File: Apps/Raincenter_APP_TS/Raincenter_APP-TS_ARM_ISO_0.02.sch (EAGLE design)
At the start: 26 parts

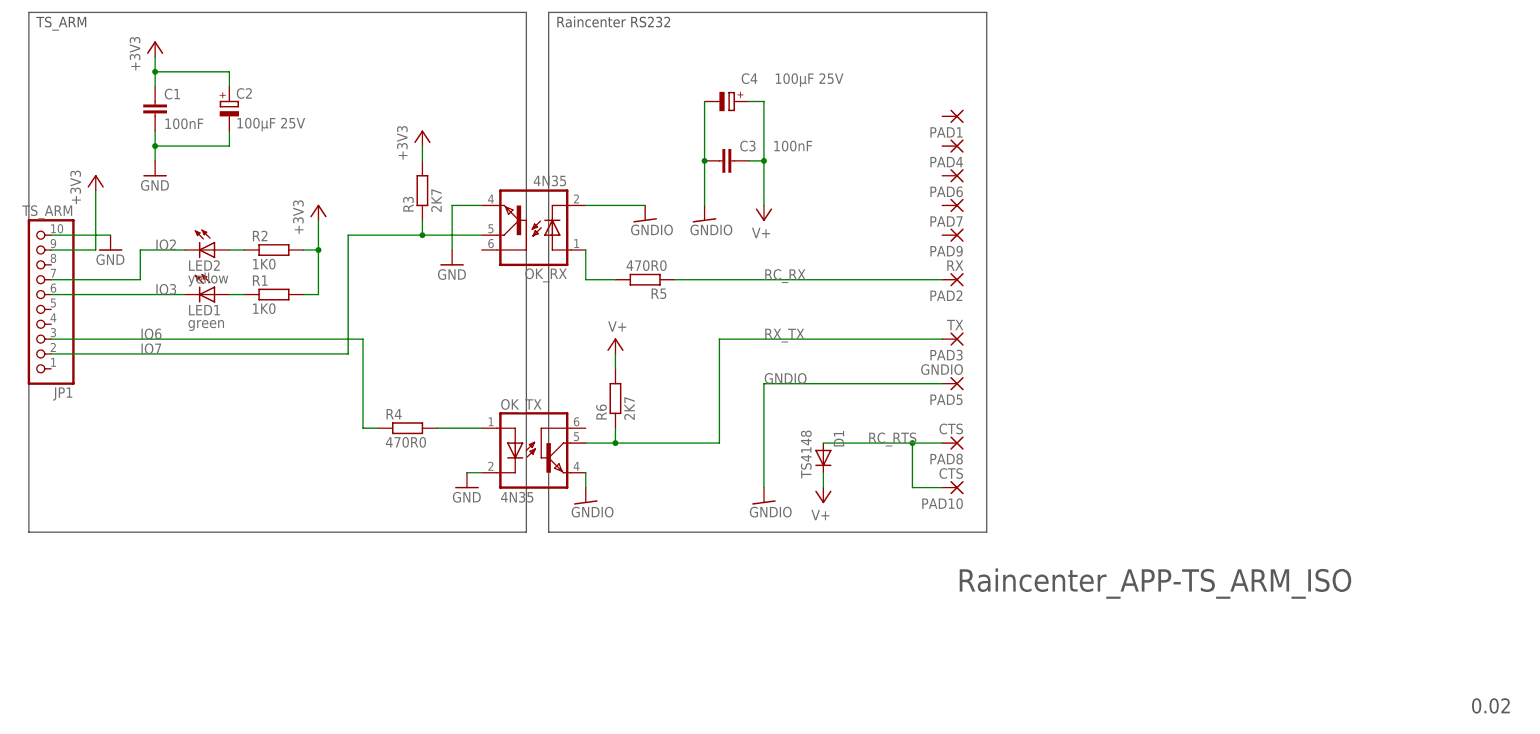
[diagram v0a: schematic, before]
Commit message: Raincenter App: positioned tNames & bNames for production
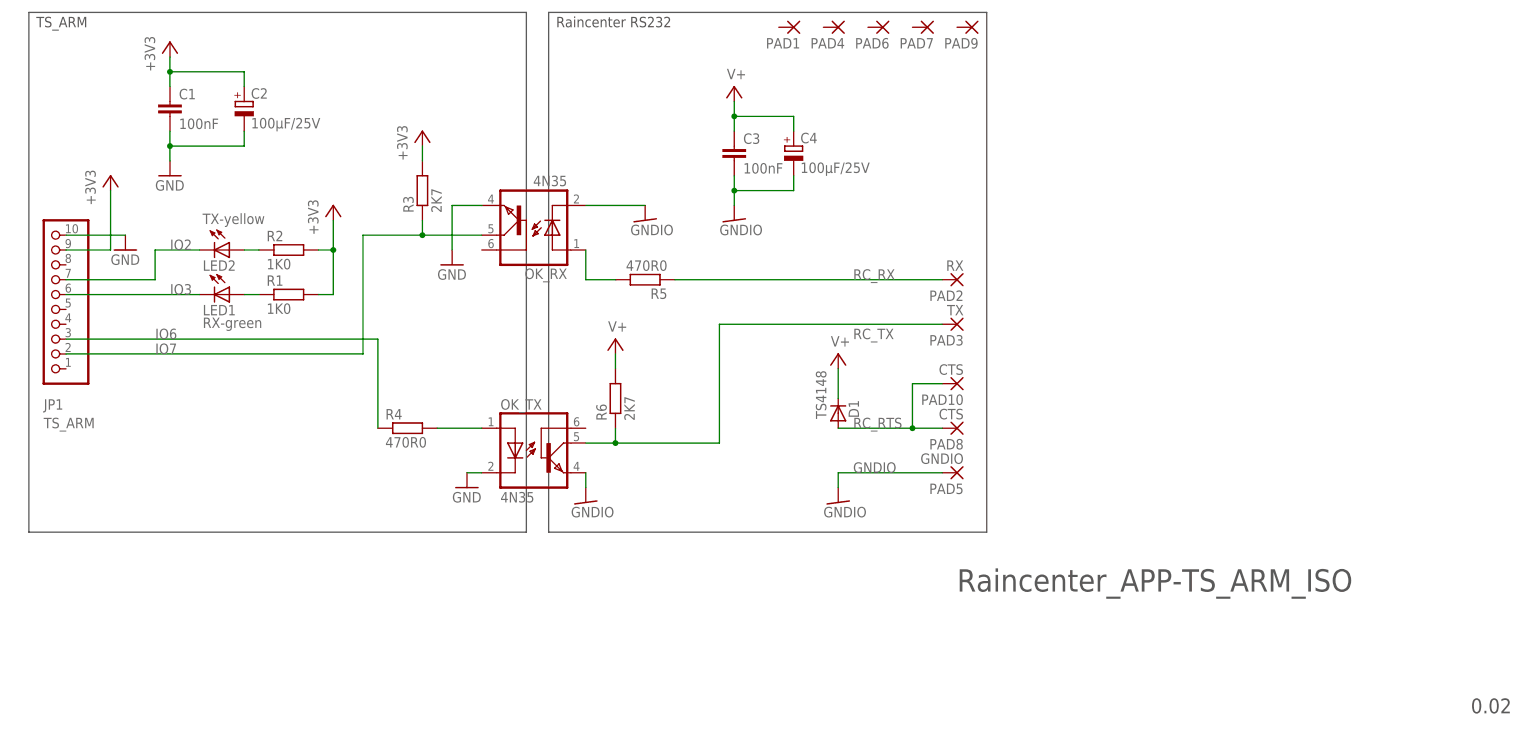
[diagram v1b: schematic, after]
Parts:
- C1, C3: OC_REICHELT (none) -> X7R-G1206 100N
- C2, C4: value 100µF 25V -> 100µF/25V
- D1: OC_REICHELT (none) -> TS 4148-1206
- LED1: value green -> RX-green; OC_REICHELT (none) -> SMD-LED 1206 GN; REICHELT SMD-LED 1206 GN -> (none)
- LED2: value yellow -> TX-yellow; OC_REICHELT (none) -> SMD-LED 1206 GE; REICHELT SMD-LED 1206 GE -> (none)
- OK_RX, OK_TX: OC_REICHELT (none) -> 4N 35
- R1, R2: OC_REICHELT (none) -> RND 1206 1 1,0K; REICHELT RND 1206 1 1,0K -> (none)
- R3: OC_REICHELT (none) -> RND 1206 1 2,7K; REICHELT RND 1206 1 4,7K -> (none)
- R4, R5: OC_REICHELT (none) -> RND 1206 1 470; REICHELT RND 1206 1 470 -> (none)
- R6: OC_REICHELT (none) -> RND 1206 1 2,7K; REICHELT RND 1206 1 3,9K -> (none)
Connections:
- net RX_TX renamed RC_TX
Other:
- moved on the sheet: C1, C2, C3, C4, D1, JP1, LED1, LED2, PAD1, PAD10, PAD3, PAD4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
